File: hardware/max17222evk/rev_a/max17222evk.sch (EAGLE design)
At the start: 20 parts, among them U1 MAX17222, U2 MAX17222

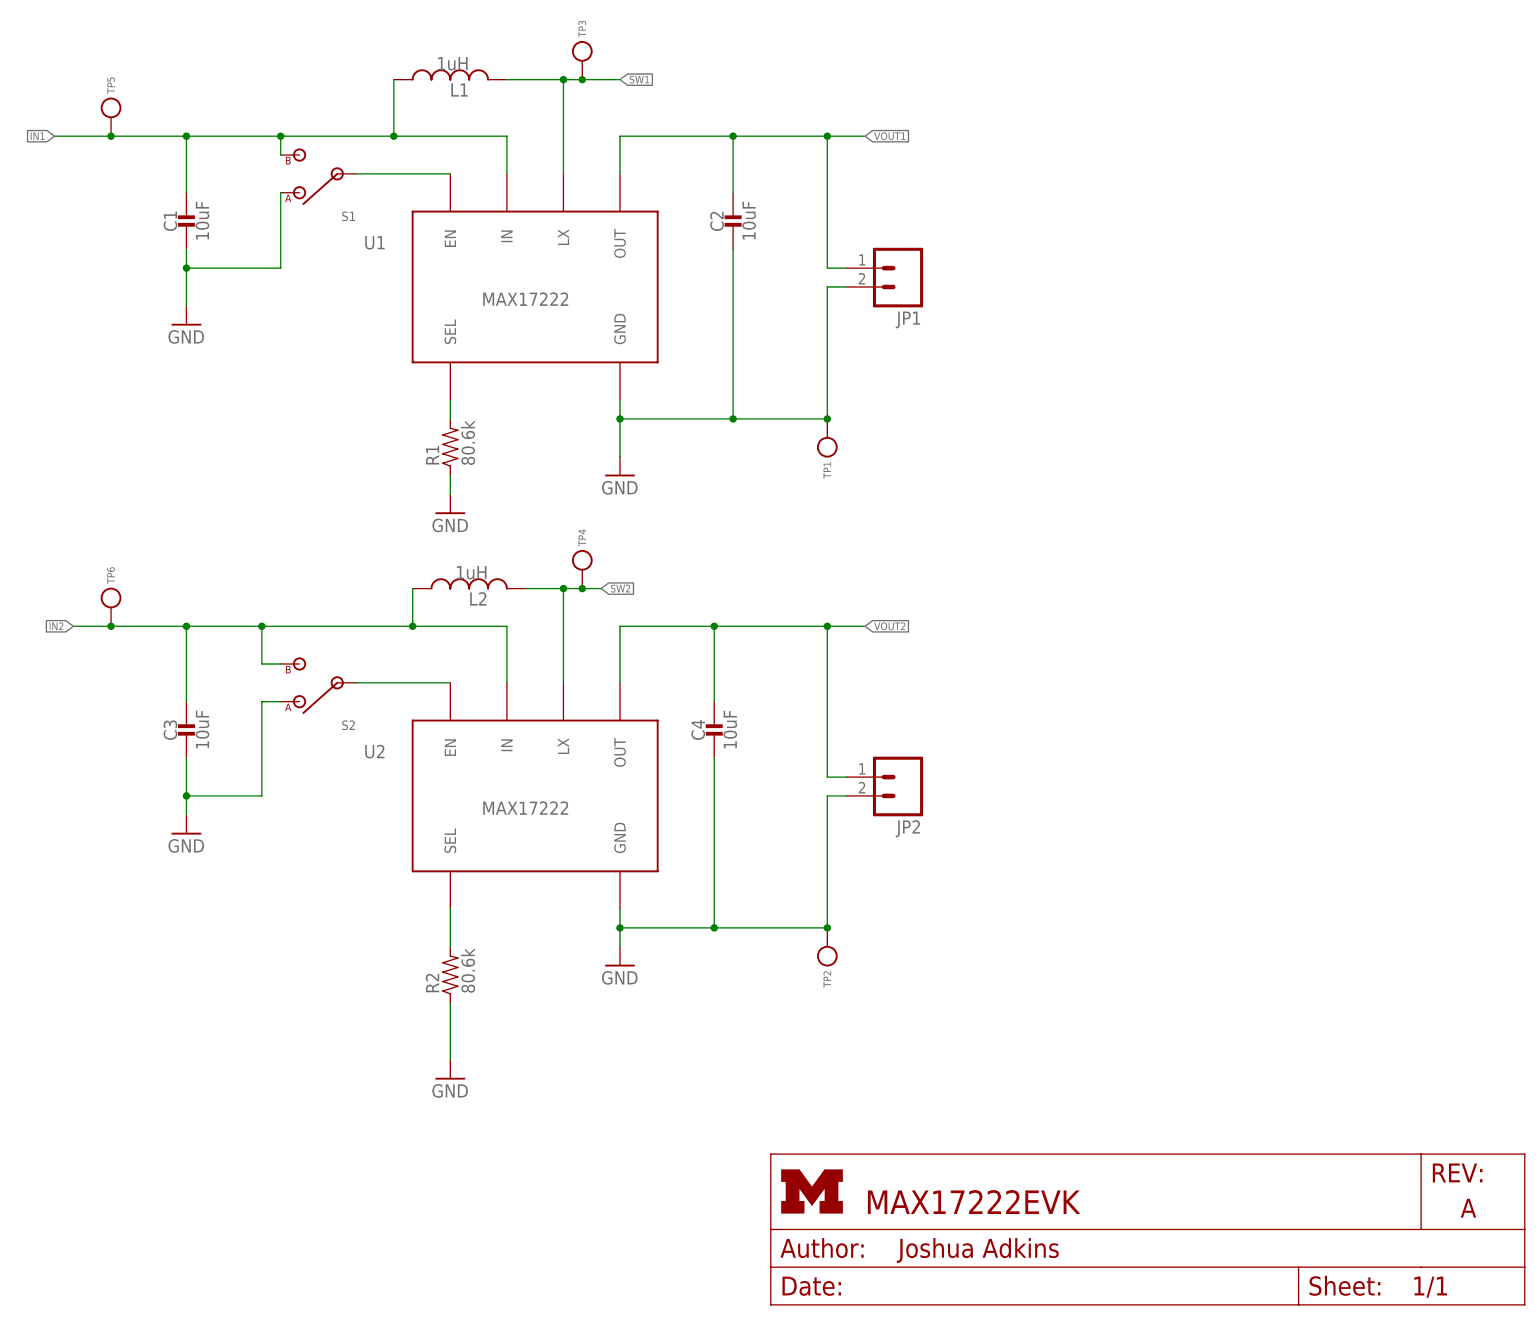
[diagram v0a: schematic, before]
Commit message: routed board, flipped load screw terminals
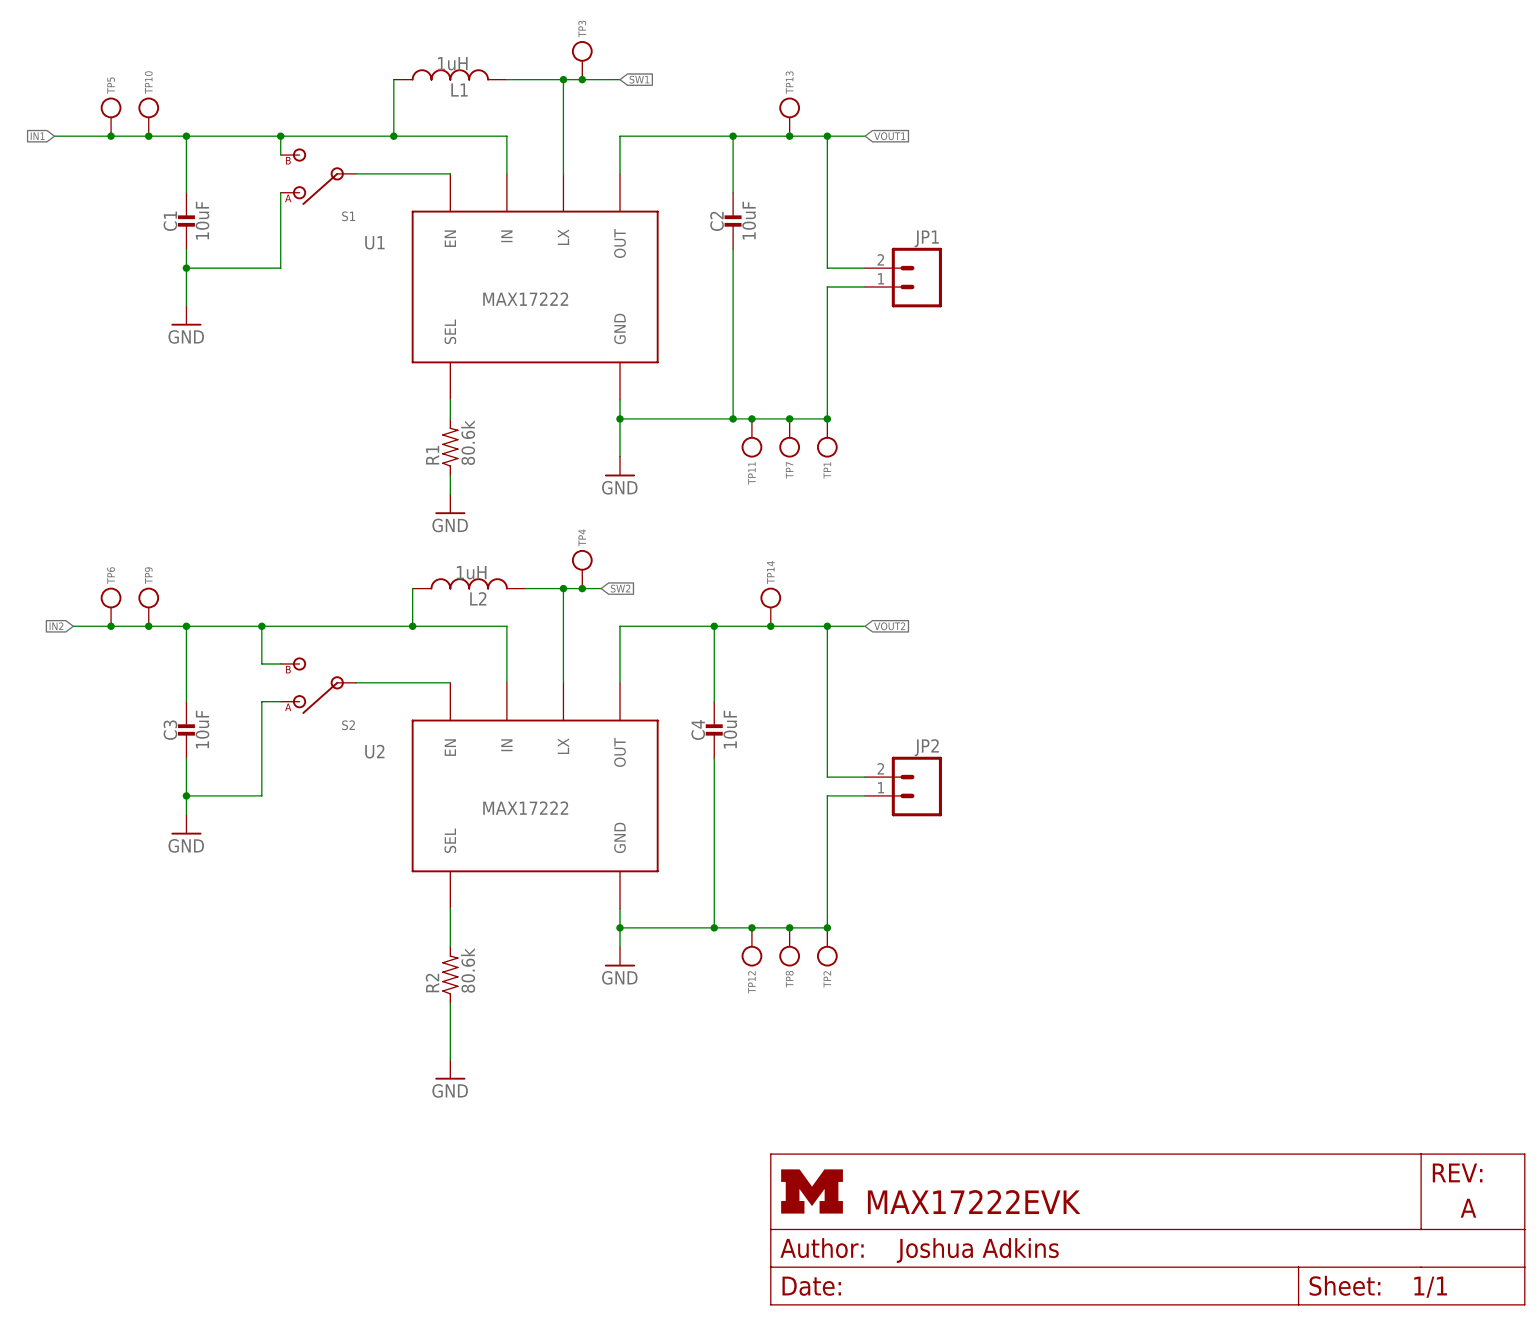
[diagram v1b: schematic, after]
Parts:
- added TP10, TP13, TP14, TP7, TP8, TP9: TEST_POINT_0.040IN, headers:TEST_POINT_0.040IN
- added TP11, TP12: TEST_POINT_0.112IN, headers:TEST_POINT_0.112IN
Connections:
- net GND: now also JP1.1, JP2.1, TP11.TESTPOINT, TP12.TESTPOINT, TP7.TESTPOINT, TP8.TESTPOINT; no longer JP1.2, JP2.2
- net IN1: now also TP10.TESTPOINT
- net IN2: now also TP9.TESTPOINT
- net VOUT1: now also JP1.2, TP13.TESTPOINT; no longer JP1.1
- net VOUT2: now also JP2.2, TP14.TESTPOINT; no longer JP2.1
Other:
- moved on the sheet: JP1, JP2
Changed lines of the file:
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@@
 <part name="TP5" library="headers" deviceset="TEST_POINT_0.040IN" device=""/>
 <part name="TP6" library="headers" deviceset="TEST_POINT_0.040IN" device=""/>
+<part name="TP7" library="headers" deviceset="TEST_POINT_0.040IN" device=""/>
+<part name="TP8" library="headers" deviceset="TEST_POINT_0.040IN" device=""/>
+<part name="TP9" library="headers" deviceset="TEST_POINT_0.040IN" device=""/>
+<part name="TP10" library="headers" deviceset="TEST_POINT_0.040IN" device=""/>
+<part name="TP11" library="headers" deviceset="TEST_POINT_0.112IN" device=""/>
+<part name="TP12" library="headers" deviceset="TEST_POINT_0.112IN" device=""/>
+<part name="TP13" library="headers" deviceset="TEST_POINT_0.040IN" device=""/>
+<part name="TP14" library="headers" deviceset="TEST_POINT_0.040IN" device=""/>
 </parts>
 <sheets>
@@
 <instance part="GND5" gate="1" x="73.66" y="132.08"/>
 <instance part="GND6" gate="1" x="73.66" y="63.5"/>
-<instance part="JP1" gate="G$1" x="170.18" y="139.7" rot="R180"/>
-<instance part="JP2" gate="G$1" x="170.18" y="71.12" rot="R180"/>
+<instance part="JP1" gate="G$1" x="172.72" y="137.16" rot="MR0"/>
+<instance part="JP2" gate="G$1" x="172.72" y="68.58" rot="MR0"/>
 <instance part="TP1" gate="G$1" x="160.02" y="116.84" rot="R90"/>
 <instance part="TP2" gate="G$1" x="160.02" y="48.26" rot="R90"/>
@@
 <instance part="TP5" gate="G$1" x="63.5" y="160.02" rot="R270"/>
 <instance part="TP6" gate="G$1" x="63.5" y="93.98" rot="R270"/>
+<instance part="TP7" gate="G$1" x="154.94" y="116.84" rot="R90"/>
+<instance part="TP8" gate="G$1" x="154.94" y="48.26" rot="R90"/>
+<instance part="TP9" gate="G$1" x="68.58" y="93.98" rot="R270"/>
+<instance part="TP10" gate="G$1" x="68.58" y="160.02" rot="R270"/>
+<instance part="TP11" gate="G$1" x="149.86" y="116.84" rot="R90"/>
+<instance part="TP12" gate="G$1" x="149.86" y="48.26" rot="R90"/>
+<instance part="TP13" gate="G$1" x="154.94" y="160.02" rot="R270"/>
+<instance part="TP14" gate="G$1" x="152.4" y="93.98" rot="R270"/>
 </instances>
 <busses>
@@
 <wire x1="101.6" y1="157.48" x2="86.36" y2="157.48" width="0.1524" layer="91"/>
 <wire x1="86.36" y1="157.48" x2="73.66" y2="157.48" width="0.1524" layer="91"/>
-<wire x1="73.66" y1="157.48" x2="63.5" y2="157.48" width="0.1524" layer="91"/>
+<wire x1="73.66" y1="157.48" x2="68.58" y2="157.48" width="0.1524" layer="91"/>
+<wire x1="68.58" y1="157.48" x2="63.5" y2="157.48" width="0.1524" layer="91"/>
 <wire x1="63.5" y1="157.48" x2="55.88" y2="157.48" width="0.1524" layer="91"/>
 <wire x1="73.66" y1="149.86" x2="73.66" y2="157.48" width="0.1524" layer="91"/>
@@
 <pinref part="TP5" gate="G$1" pin="TESTPOINT"/>
 <junction x="63.5" y="157.48"/>
+<pinref part="TP10" gate="G$1" pin="TESTPOINT"/>
+<junction x="68.58" y="157.48"/>
 </segment>
 </net>
@@
 <wire x1="147.32" y1="119.38" x2="147.32" y2="142.24" width="0.1524" layer="91"/>
 <junction x="132.08" y="119.38"/>
-<pinref part="JP1" gate="G$1" pin="2"/>
-<wire x1="162.56" y1="137.16" x2="160.02" y2="137.16" width="0.1524" layer="91"/>
 <wire x1="160.02" y1="137.16" x2="160.02" y2="119.38" width="0.1524" layer="91"/>
-<wire x1="160.02" y1="119.38" x2="147.32" y2="119.38" width="0.1524" layer="91"/>
 <junction x="147.32" y="119.38"/>
 <pinref part="TP1" gate="G$1" pin="TESTPOINT"/>
 <junction x="160.02" y="119.38"/>
+<pinref part="JP1" gate="G$1" pin="1"/>
+<wire x1="160.02" y1="119.38" x2="154.94" y2="119.38" width="0.1524" layer="91"/>
+<wire x1="154.94" y1="119.38" x2="149.86" y2="119.38" width="0.1524" layer="91"/>
+<wire x1="149.86" y1="119.38" x2="147.32" y2="119.38" width="0.1524" layer="91"/>
+<wire x1="160.02" y1="137.16" x2="165.1" y2="137.16" width="0.1524" layer="91"/>
+<pinref part="TP7" gate="G$1" pin="TESTPOINT"/>
+<junction x="154.94" y="119.38"/>
+<pinref part="TP11" gate="G$1" pin="TESTPOINT"/>
+<junction x="149.86" y="119.38"/>
 </segment>
 <segment>
@@
 <wire x1="144.78" y1="50.8" x2="132.08" y2="50.8" width="0.1524" layer="91"/>
 <junction x="132.08" y="50.8"/>
-<pinref part="JP2" gate="G$1" pin="2"/>
-<wire x1="162.56" y1="68.58" x2="160.02" y2="68.58" width="0.1524" layer="91"/>
 <wire x1="160.02" y1="68.58" x2="160.02" y2="50.8" width="0.1524" layer="91"/>
-<wire x1="160.02" y1="50.8" x2="144.78" y2="50.8" width="0.1524" layer="91"/>
 <junction x="144.78" y="50.8"/>
 <pinref part="TP2" gate="G$1" pin="TESTPOINT"/>
 <junction x="160.02" y="50.8"/>
+<pinref part="JP2" gate="G$1" pin="1"/>
+<wire x1="160.02" y1="50.8" x2="154.94" y2="50.8" width="0.1524" layer="91"/>
+<wire x1="154.94" y1="50.8" x2="149.86" y2="50.8" width="0.1524" layer="91"/>
+<wire x1="149.86" y1="50.8" x2="144.78" y2="50.8" width="0.1524" layer="91"/>
+<wire x1="160.02" y1="68.58" x2="165.1" y2="68.58" width="0.1524" layer="91"/>
+<pinref part="TP8" gate="G$1" pin="TESTPOINT"/>
+<junction x="154.94" y="50.8"/>
+<pinref part="TP12" gate="G$1" pin="TESTPOINT"/>
+<junction x="149.86" y="50.8"/>
 </segment>
 </net>
@@
 <pinref part="C2" gate="G$1" pin="1"/>
 <wire x1="147.32" y1="149.86" x2="147.32" y2="157.48" width="0.1524" layer="91"/>
-<wire x1="147.32" y1="157.48" x2="160.02" y2="157.48" width="0.1524" layer="91"/>
+<wire x1="147.32" y1="157.48" x2="154.94" y2="157.48" width="0.1524" layer="91"/>
+<wire x1="154.94" y1="157.48" x2="160.02" y2="157.48" width="0.1524" layer="91"/>
 <wire x1="160.02" y1="157.48" x2="160.02" y2="139.7" width="0.1524" layer="91"/>
 <junction x="147.32" y="157.48"/>
-<pinref part="JP1" gate="G$1" pin="1"/>
-<wire x1="160.02" y1="139.7" x2="162.56" y2="139.7" width="0.1524" layer="91"/>
 <wire x1="160.02" y1="157.48" x2="165.1" y2="157.48" width="0.1524" layer="91"/>
 <junction x="160.02" y="157.48"/>
 <label x="165.1" y="157.48" size="1.016" layer="95" xref="yes"/>
+<pinref part="JP1" gate="G$1" pin="2"/>
+<wire x1="160.02" y1="139.7" x2="165.1" y2="139.7" width="0.1524" layer="91"/>
+<pinref part="TP13" gate="G$1" pin="TESTPOINT"/>
+<junction x="154.94" y="157.48"/>
 </segment>
 </net>
@@
 <wire x1="104.14" y1="96.52" x2="104.14" y2="91.44" width="0.1524" layer="91"/>
 <junction x="104.14" y="91.44"/>
-<wire x1="73.66" y1="91.44" x2="63.5" y2="91.44" width="0.1524" layer="91"/>
+<wire x1="73.66" y1="91.44" x2="68.58" y2="91.44" width="0.1524" layer="91"/>
 <junction x="73.66" y="91.44"/>
 <label x="58.42" y="91.44" size="1.016" layer="95" rot="R180" xref="yes"/>
 <pinref part="TP6" gate="G$1" pin="TESTPOINT"/>
+<wire x1="68.58" y1="91.44" x2="63.5" y2="91.44" width="0.1524" layer="91"/>
 <wire x1="63.5" y1="91.44" x2="58.42" y2="91.44" width="0.1524" layer="91"/>
 <junction x="63.5" y="91.44"/>
+<pinref part="TP9" gate="G$1" pin="TESTPOINT"/>
+<junction x="68.58" y="91.44"/>
 </segment>
 </net>
@@
 <wire x1="132.08" y1="91.44" x2="144.78" y2="91.44" width="0.1524" layer="91"/>
 <pinref part="C4" gate="G$1" pin="1"/>
-<wire x1="144.78" y1="91.44" x2="160.02" y2="91.44" width="0.1524" layer="91"/>
+<wire x1="144.78" y1="91.44" x2="152.4" y2="91.44" width="0.1524" layer="91"/>
+<wire x1="152.4" y1="91.44" x2="160.02" y2="91.44" width="0.1524" layer="91"/>
 <wire x1="144.78" y1="81.28" x2="144.78" y2="91.44" width="0.1524" layer="91"/>
 <junction x="144.78" y="91.44"/>
-<pinref part="JP2" gate="G$1" pin="1"/>
-<wire x1="162.56" y1="71.12" x2="160.02" y2="71.12" width="0.1524" layer="91"/>
 <wire x1="160.02" y1="71.12" x2="160.02" y2="91.44" width="0.1524" layer="91"/>
 <wire x1="160.02" y1="91.44" x2="165.1" y2="91.44" width="0.1524" layer="91"/>
 <junction x="160.02" y="91.44"/>
 <label x="165.1" y="91.44" size="1.016" layer="95" xref="yes"/>
-</segment>
-</net>
+<pinref part="JP2" gate="G$1" pin="2"/>
+<wire x1="160.02" y1="71.12" x2="165.1" y2="71.12" width="0.1524" layer="91"/>
+<pinref part="TP14" gate="G$1" pin="TESTPOINT"/>
+<junction x="152.4" y="91.44"/>
+</segment>
+</net>

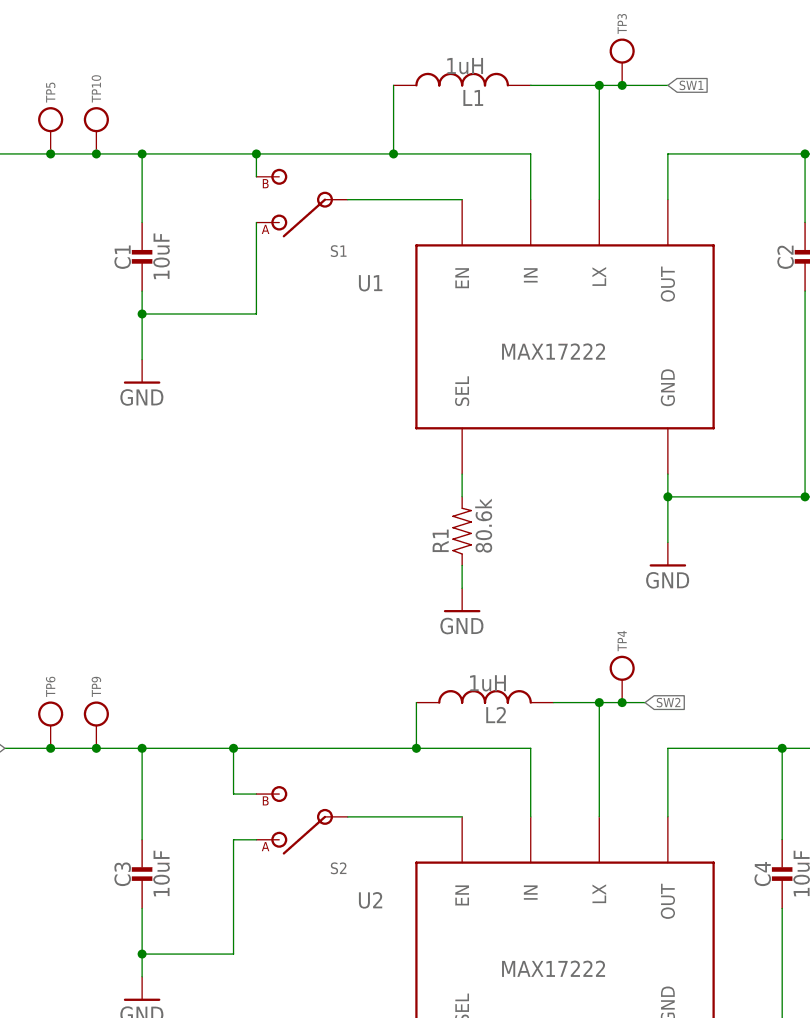
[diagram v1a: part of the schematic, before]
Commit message: added resistor to enable line
I believe this is necessary for lower power operation.
It is in maxim's EVK
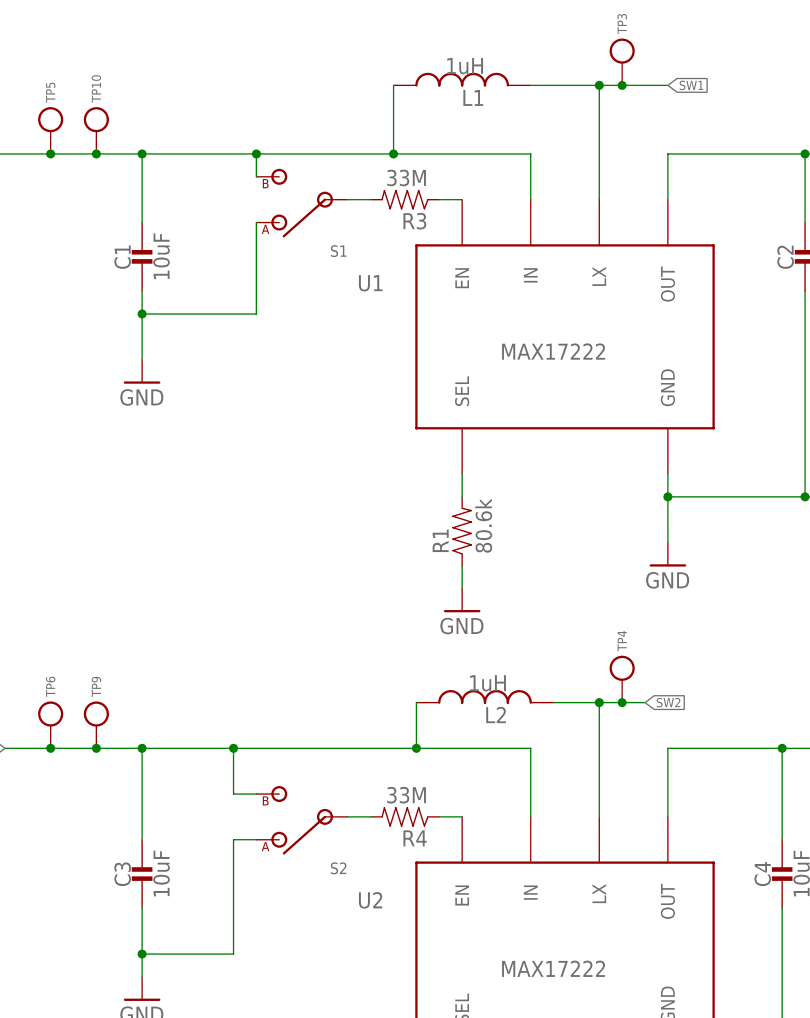
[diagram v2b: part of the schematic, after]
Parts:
- added R3, R4: 33M, passives:RESISTOR0603_RES
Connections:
- removed net N$7: S2.2, U2.EN
- new net N$1: R3.2, S1.2
- new net N$3: R4.2, S2.2
- new net N$4: R4.1, U2.EN
- net N$2: now also R3.1; no longer S1.2
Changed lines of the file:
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@@
 <part name="TP13" library="headers" deviceset="TEST_POINT_0.040IN" device=""/>
 <part name="TP14" library="headers" deviceset="TEST_POINT_0.040IN" device=""/>
+<part name="R3" library="passives" deviceset="RESISTOR" device="0603_RES" value="33M"/>
+<part name="R4" library="passives" deviceset="RESISTOR" device="0603_RES" value="33M"/>
 </parts>
 <sheets>
@@
 <instance part="TP13" gate="G$1" x="154.94" y="160.02" rot="R270"/>
 <instance part="TP14" gate="G$1" x="152.4" y="93.98" rot="R270"/>
+<instance part="R3" gate="G$1" x="101.6" y="152.4" rot="R180"/>
+<instance part="R4" gate="G$1" x="101.6" y="83.82" rot="R180"/>
 </instances>
 <busses>
@@
 <pinref part="TP12" gate="G$1" pin="TESTPOINT"/>
 <junction x="149.86" y="50.8"/>
-</segment>
-</net>
-<net name="N$2" class="0">
-<segment>
-<pinref part="S1" gate="G$1" pin="2"/>
-<pinref part="U1" gate="G$1" pin="EN"/>
-<wire x1="96.52" y1="152.4" x2="109.22" y2="152.4" width="0.1524" layer="91"/>
 </segment>
 </net>
@@
 </segment>
 </net>
-<net name="N$7" class="0">
-<segment>
-<pinref part="S2" gate="G$1" pin="2"/>
-<pinref part="U2" gate="G$1" pin="EN"/>
-<wire x1="96.52" y1="83.82" x2="109.22" y2="83.82" width="0.1524" layer="91"/>
-</segment>
-</net>
 <net name="SW2" class="0">
 <segment>
@@
 </segment>
 </net>
+<net name="N$1" class="0">
+<segment>
+<pinref part="S1" gate="G$1" pin="2"/>
+<pinref part="R3" gate="G$1" pin="2"/>
+<wire x1="96.52" y1="152.4" x2="99.06" y2="152.4" width="0.1524" layer="91"/>
+</segment>
+</net>
+<net name="N$2" class="0">
+<segment>
+<pinref part="R3" gate="G$1" pin="1"/>
+<pinref part="U1" gate="G$1" pin="EN"/>
+<wire x1="106.68" y1="152.4" x2="109.22" y2="152.4" width="0.1524" layer="91"/>
+</segment>
+</net>
+<net name="N$3" class="0">
+<segment>
+<pinref part="S2" gate="G$1" pin="2"/>
+<pinref part="R4" gate="G$1" pin="2"/>
+<wire x1="96.52" y1="83.82" x2="99.06" y2="83.82" width="0.1524" layer="91"/>
+</segment>
+</net>
+<net name="N$4" class="0">
+<segment>
+<pinref part="R4" gate="G$1" pin="1"/>
+<pinref part="U2" gate="G$1" pin="EN"/>
+<wire x1="106.68" y1="83.82" x2="109.22" y2="83.82" width="0.1524" layer="91"/>
+</segment>
+</net>
